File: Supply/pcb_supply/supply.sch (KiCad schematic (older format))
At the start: 31 parts, among them J1 Screw_Terminal_01x02, J2 Screw_Terminal_01x02, Q1 FDS4685, U1 LTC3864

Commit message: Comienzo con la 3ra revisión de la fuente de switching
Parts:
- removed C13: 22p, Capacitor_SMD:C_0805_2012Metric, symbol Device:C
- removed R1: 390K, Resistor_SMD:R_0805_2012Metric, symbol Device:R
- removed R11: 0, Resistor_SMD:R_0805_2012Metric, symbol Device:R
- removed R2: 33K, Resistor_SMD:R_0805_2012Metric, symbol Device:R
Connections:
- no-connect marks 1 -> 2
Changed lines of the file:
@@
-$EndComp
-$Comp
-L power:GND #PWR0102
-U 1 1 5CF50B5F
-P 1800 4150
-F 0 "#PWR0102" H 1800 3900 50  0001 C CNN
-F 1 "GND" H 1805 3977 50  0000 C CNN
-F 2 "" H 1800 4150 50  0001 C CNN
-F 3 "" H 1800 4150 50  0001 C CNN
-	1    1800 4150
-	1    0    0    -1
 $EndComp
 $Comp
@@
 $EndComp
 $Comp
-L Device:R R2
-U 1 1 5CF56FE7
-P 1800 3950
-F 0 "R2" H 1870 3996 50  0000 L CNN
-F 1 "33K" H 1870 3905 50  0000 L CNN
-F 2 "Resistor_SMD:R_0805_2012Metric" V 1730 3950 50  0001 C CNN
-F 3 "~" H 1800 3950 50  0001 C CNN
-	1    1800 3950
-	1    0    0    -1
-$EndComp
-Wire Wire Line
-	1800 3600 1800 3700
-Connection ~ 1800 3700
-Wire Wire Line
-	1800 3700 1800 3800
-$Comp
 L Device:C C3
 U 1 1 5CF5D44F
@@
 	3300 4250 3300 4400
 $Comp
-L Device:R R1
-U 1 1 5CF567F1
-P 1800 3450
-F 0 "R1" H 1870 3496 50  0000 L CNN
-F 1 "390K" H 1870 3405 50  0000 L CNN
-F 2 "Resistor_SMD:R_0805_2012Metric" V 1730 3450 50  0001 C CNN
-F 3 "~" H 1800 3450 50  0001 C CNN
-	1    1800 3450
-	1    0    0    -1
-$EndComp
-$Comp
 L power:GND #PWR0103
 U 1 1 5CF4FB12
@@
 F 3 "" H 3600 5000 50  0001 C CNN
 	1    3600 5000
-	1    0    0    -1
-$EndComp
-Wire Wire Line
-	1800 3300 1800 3200
-$Comp
-L power:VDC #PWR0109
-U 1 1 5CF71197
-P 1800 2900
-F 0 "#PWR0109" H 1800 2800 50  0001 C CNN
-F 1 "VDC" H 1800 3175 50  0000 C CNN
-F 2 "" H 1800 2900 50  0001 C CNN
-F 3 "" H 1800 2900 50  0001 C CNN
-	1    1800 2900
 	1    0    0    -1
 $EndComp
@@
 Wire Wire Line
 	3150 3800 3100 3800
-Wire Wire Line
-	1800 4100 1800 4150
 $Comp
 L Device:LED D2
@@
 Wire Wire Line
 	4300 3300 4300 3400
-Wire Wire Line
-	3600 3700 1800 3700
 NoConn ~ 4700 4450
 Wire Wire Line
@@
 Wire Wire Line
 	7100 4650 7100 4800
-$Comp
-L Device:R R11
-U 1 1 5D0DF114
-P 1800 3050
-F 0 "R11" H 1950 3100 50  0000 C CNN
-F 1 "0" H 1900 3000 50  0000 C CNN
-F 2 "Resistor_SMD:R_0805_2012Metric" V 1730 3050 50  0001 C CNN
-F 3 "~" H 1800 3050 50  0001 C CNN
-	1    1800 3050
-	1    0    0    -1
-$EndComp
 $Comp
 L Device:C C12
@@
 	0    1    1    0
 $EndComp
-$Comp
-L Device:C C13
-U 1 1 5D334CAA
-P 4900 4250
-F 0 "C13" H 5100 4300 50  0000 C CNN
-F 1 "22p" H 5100 4200 50  0000 C CNN
-F 2 "Capacitor_SMD:C_0805_2012Metric" H 4938 4100 50  0001 C CNN
-F 3 "~" H 4900 4250 50  0001 C CNN
-	1    4900 4250
-	1    0    0    -1
-$EndComp
-$Comp
-L power:GND #PWR05
-U 1 1 5D335227
-P 4900 4450
-F 0 "#PWR05" H 4900 4200 50  0001 C CNN
-F 1 "GND" H 5000 4350 50  0000 C CNN
-F 2 "" H 4900 4450 50  0001 C CNN
-F 3 "" H 4900 4450 50  0001 C CNN
-	1    4900 4450
-	1    0    0    -1
-$EndComp
-Wire Wire Line
-	4900 4100 4900 4000
-Connection ~ 4900 4000
-Wire Wire Line
-	4900 4400 4900 4450
+NoConn ~ 3600 3700
 $EndSCHEMATC

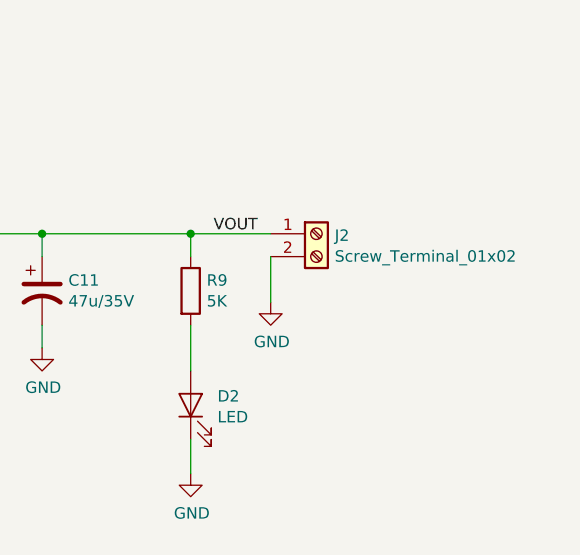
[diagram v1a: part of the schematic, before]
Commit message: Comienzo con la 3ra revisión de la fuente de switching(2)
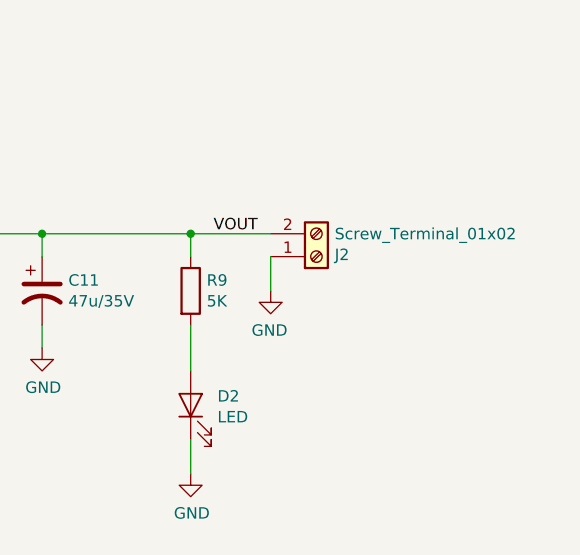
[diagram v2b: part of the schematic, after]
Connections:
- net GND: now also J2.1 (Pin_1); no longer J2.2 (Pin_2)
- net VOUT: now also J2.2 (Pin_2); no longer J2.1 (Pin_1)
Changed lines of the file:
@@
 Wire Wire Line
 	8750 4700 8750 4600
-Wire Wire Line
-	9400 4200 9750 4200
 Connection ~ 9400 4200
-$Comp
-L power:GND #PWR03
-U 1 1 5D0440E7
-P 9750 4500
-F 0 "#PWR03" H 9750 4250 50  0001 C CNN
-F 1 "GND" H 9755 4327 50  0000 C CNN
-F 2 "" H 9750 4500 50  0001 C CNN
-F 3 "" H 9750 4500 50  0001 C CNN
-	1    9750 4500
-	1    0    0    -1
-$EndComp
 $Comp
 L power:GND #PWR0117
@@
 	-1   0    0    -1
 $EndComp
-$Comp
-L Connector:Screw_Terminal_01x02 J2
-U 1 1 5D065E71
-P 9950 4200
-F 0 "J2" H 10030 4192 50  0000 L CNN
-F 1 "Screw_Terminal_01x02" H 10030 4101 50  0000 L CNN
-F 2 "Connector:691102710002" H 9950 4200 50  0001 C CNN
-F 3 "~" H 9950 4200 50  0001 C CNN
-	1    9950 4200
-	1    0    0    -1
-$EndComp
 Wire Wire Line
 	1100 4150 1100 4350
-Wire Wire Line
-	9750 4300 9750 4500
 Wire Wire Line
 	6700 4200 7100 4200
@@
 $EndComp
 NoConn ~ 3600 3700
+Wire Wire Line
+	9400 4200 9750 4200
+$Comp
+L power:GND #PWR03
+U 1 1 5D0440E7
+P 9750 4450
+F 0 "#PWR03" H 9750 4200 50  0001 C CNN
+F 1 "GND" H 9755 4277 50  0000 C CNN
+F 2 "" H 9750 4450 50  0001 C CNN
+F 3 "" H 9750 4450 50  0001 C CNN
+	1    9750 4450
+	-1   0    0    -1
+$EndComp
+$Comp
+L Connector:Screw_Terminal_01x02 J2
+U 1 1 5D065E71
+P 9950 4300
+F 0 "J2" H 10030 4292 50  0000 L CNN
+F 1 "Screw_Terminal_01x02" H 10030 4201 50  0000 L CNN
+F 2 "Connector:691102710002" H 9950 4300 50  0001 C CNN
+F 3 "~" H 9950 4300 50  0001 C CNN
+	1    9950 4300
+	1    0    0    1
+$EndComp
+Wire Wire Line
+	9750 4300 9750 4450
 $EndSCHEMATC
